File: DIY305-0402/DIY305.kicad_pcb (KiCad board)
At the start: 2 copper layers, 9.8 x 18.5 mm, 37 parts

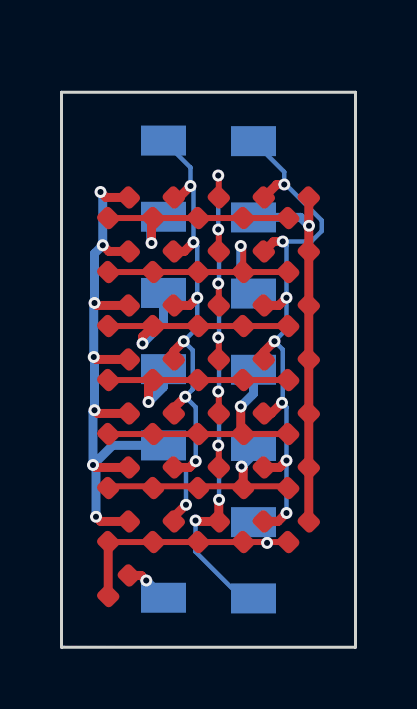
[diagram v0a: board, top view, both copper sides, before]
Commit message: Removal of old design
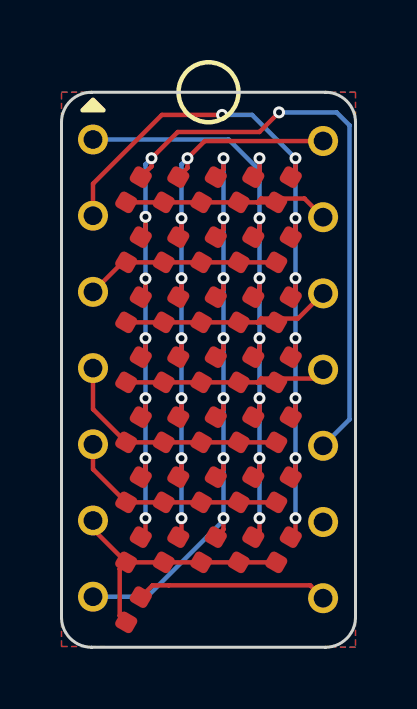
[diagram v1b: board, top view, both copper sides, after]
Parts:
- removed REF**: PinHeader_2x07_P2.54mm_Vertical_SMD, Connector_PinHeader_2.54mm:PinHeader_2x07_P2.54mm_Vertical_SMD
- added J1: Conn_01x07, Connector_PinHeader_2.54mm:PinHeader_1x07_P2.54mm_Vertical, F.Cu at (21.1, 21.6)
- added J2: Conn_01x07, Connector_PinHeader_2.54mm:PinHeader_1x07_P2.54mm_Vertical, F.Cu at (28.7, 21.6)
- moved D36 0.94 mm to (22.4, 37.2), turned to 60 degrees
- moved D1 0.78 mm to (22.4, 23.2), turned to 60 degrees
- moved D29 0.78 mm to (27.4, 23.2), turned to 60 degrees
- moved D35 0.78 mm to (27.4, 35.2), turned to 60 degrees
- moved D7 0.78 mm to (22.4, 35.2), turned to 60 degrees
- moved D14 0.65 mm to (23.6, 35.2), turned to 60 degrees
- moved D22 0.65 mm to (26.1, 23.2), turned to 60 degrees
- moved D28 0.65 mm to (26.1, 35.2), turned to 60 degrees
- moved D8 0.65 mm to (23.6, 23.2), turned to 60 degrees
- moved D2 0.64 mm to (22.4, 25.2), turned to 60 degrees
- moved D30 0.64 mm to (27.4, 25.2), turned to 60 degrees
- moved D34 0.64 mm to (27.4, 33.2), turned to 60 degrees
- moved D6 0.64 mm to (22.4, 33.2), turned to 60 degrees
- moved D15 0.60 mm to (24.9, 23.2), turned to 60 degrees
- moved D21 0.60 mm to (24.9, 35.2), turned to 60 degrees
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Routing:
- net C1: track 21.6 -> 35.5 mm, vias 7 -> 8
- net C5: track 12.8 -> 26.2 mm, vias 1 -> 8
- net DP: track 1.46 -> 6.42 mm, vias 1 -> 0
- net C2: track 18.7 -> 21.6 mm
- net R2: track 9.06 -> 6.52 mm, vias 1 -> 0
- net C4: track 20.6 -> 23.0 mm
- net C3: track 20.4 -> 22.6 mm, vias 8 -> 7
- net R3: track 8.70 -> 7.59 mm, vias 1 -> 0
- net R4: track 8.10 -> 7.36 mm, vias 1 -> 0
- net R1: track 7.92 -> 7.50 mm, vias 1 -> 0
- net R5: track 8.35 -> 7.93 mm, vias 1 -> 0
- net R7: track 8.70 -> 9.03 mm, vias 1 -> 0
- net R6: track 7.64 -> 7.39 mm, vias 1 -> 0
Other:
- outline, holes or cut-outs redrawn
- board text added: "env"

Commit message: Fixed silly flip error
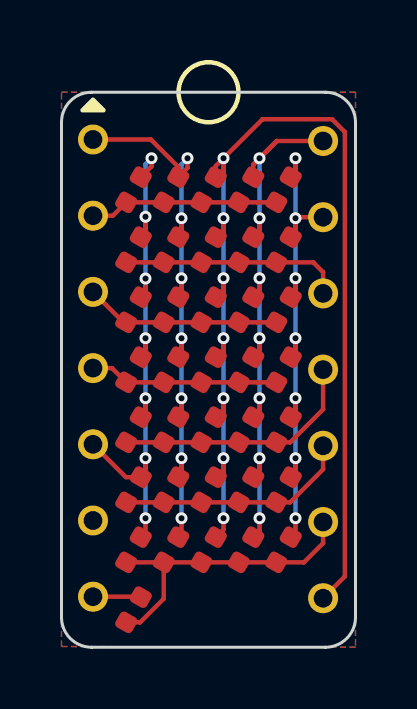
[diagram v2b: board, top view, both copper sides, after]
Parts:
- moved J1 7.67 mm to (28.7, 21.6)
- moved J2 7.67 mm to (21.1, 21.6)
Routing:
- net C1: track 35.5 -> 19.1 mm, vias 8 -> 7
- net C3: track 22.6 -> 38.6 mm
- net C5: track 26.2 -> 17.8 mm, vias 8 -> 7
- net DP: track 6.42 -> 1.60 mm
- net C4: track 23.0 -> 20.5 mm
- net R7: track 9.03 -> 10.3 mm
- net R1: track 7.50 -> 6.29 mm
- net C2: track 21.6 -> 20.4 mm
- net R3: track 7.59 -> 6.53 mm
- net R4: track 7.36 -> 6.30 mm
- net R2: track 6.52 -> 7.53 mm

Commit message: Added iPirie's logo and corrected single trace to reduce possibility of mechanical damage to PCB
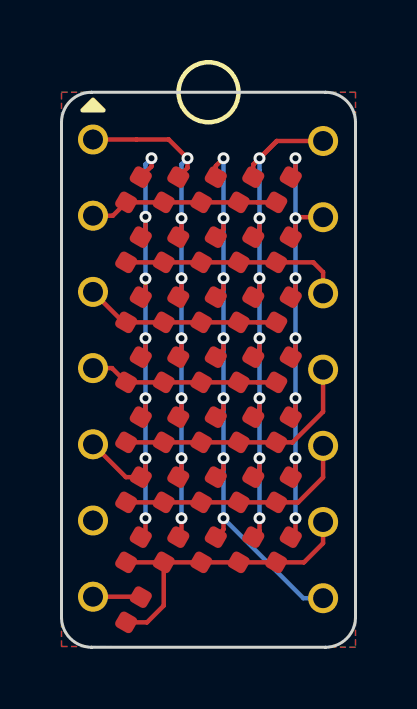
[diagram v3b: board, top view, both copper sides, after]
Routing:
- net C3: track 38.6 -> 22.0 mm
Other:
- board text added: "Ru-Pirie"

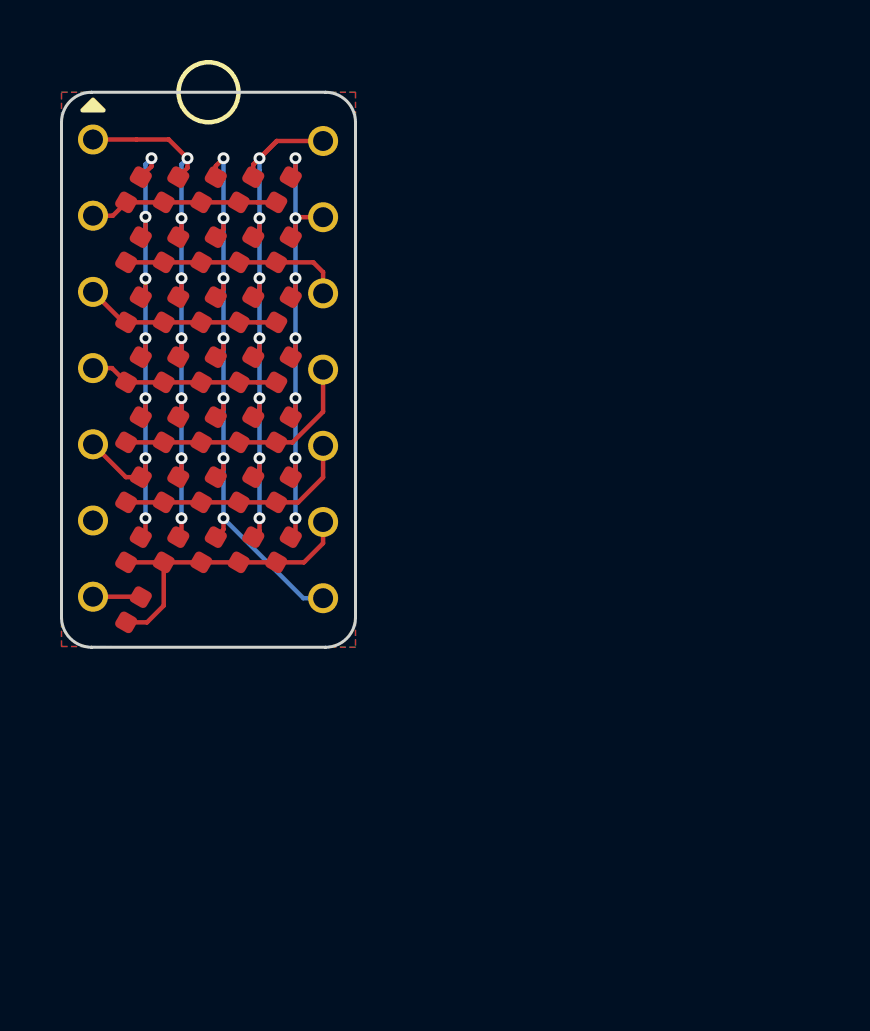
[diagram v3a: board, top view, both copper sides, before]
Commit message: Fixed spacing of pins and corrected orientation, made holes bigger and made tracks curvey with teardrops.
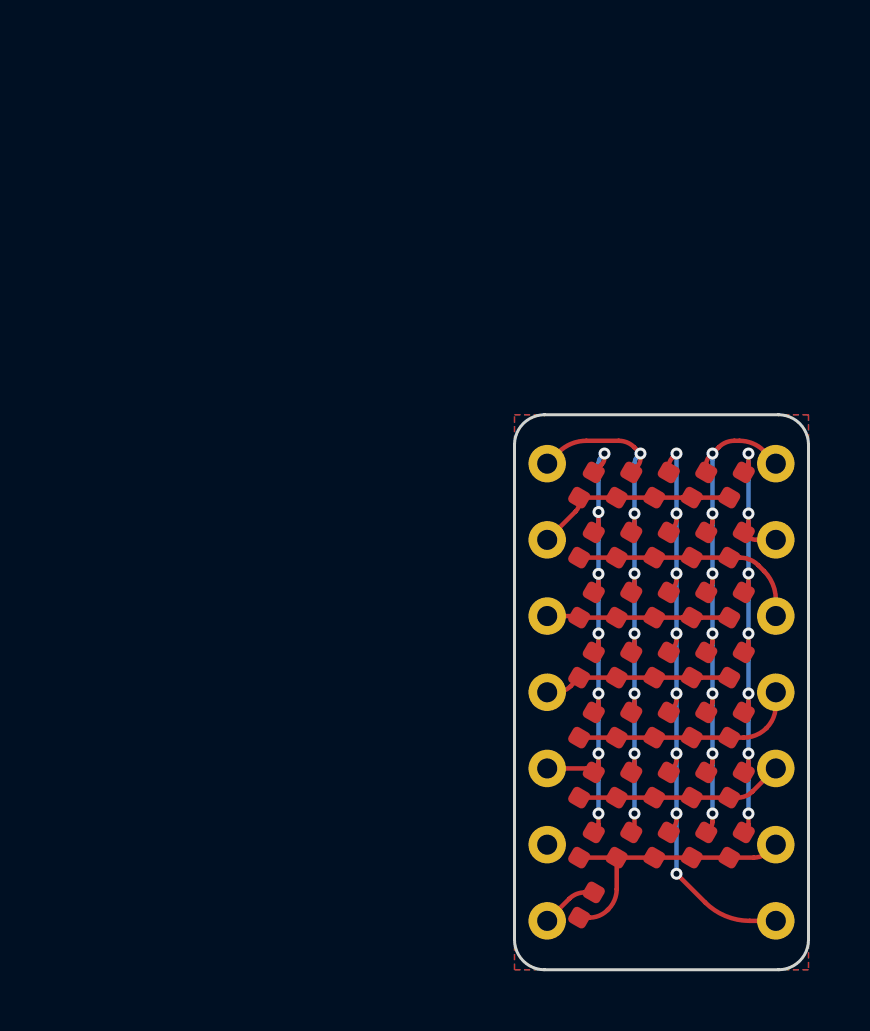
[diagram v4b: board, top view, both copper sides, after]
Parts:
- removed J1, J2: Conn_01x07, Connector_PinHeader_2.54mm:PinHeader_1x07_P2.54mm_Vertical
- added J3: Conn_01x14, Connector_PinHeader_1.00mm:PinHeader_1x14_P1.00mm_Vertical, F.Cu at (36.2, 32.4)
- moved D1 18.0 mm to (37.5, 33.1)
- moved D10 18.0 mm to (38.8, 37.1)
- moved D11 18.0 mm to (38.8, 39.1)
- moved D12 18.0 mm to (38.8, 41.1)
- moved D13 18.0 mm to (38.8, 43.1)
- moved D14 18.0 mm to (38.8, 45.1)
- moved D15 18.0 mm to (40.0, 33.1)
- moved D16 18.0 mm to (40.0, 35.1)
- moved D17 18.0 mm to (40.0, 37.1)
- moved D18 18.0 mm to (40.0, 39.1)
- moved D19 18.0 mm to (40.0, 41.1)
- moved D2 18.0 mm to (37.5, 35.1)
- moved D20 18.0 mm to (40.0, 43.1)
- moved D21 18.0 mm to (40.0, 45.1)
- moved D22 18.0 mm to (41.2, 33.1)
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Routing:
- net C4: track 20.5 -> 19.4 mm
- net R6: track 7.96 -> 6.92 mm
- net R7: track 10.5 -> 9.53 mm
- net C3: track 22.0 -> 22.9 mm, vias 7 -> 8
- net R5: track 8.39 -> 7.59 mm
- net C1: track 19.1 -> 18.6 mm
- net R1: track 6.29 -> 6.83 mm
